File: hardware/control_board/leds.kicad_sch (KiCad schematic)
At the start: 17 parts, among them Q1 2N7002A

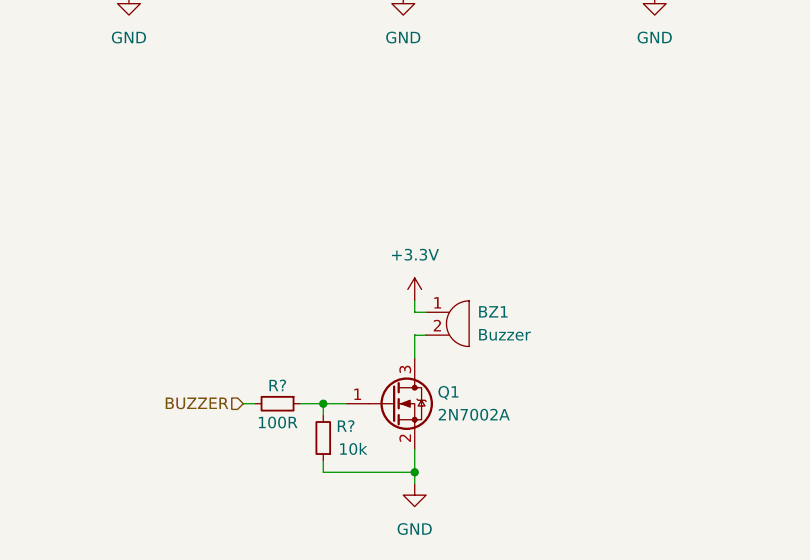
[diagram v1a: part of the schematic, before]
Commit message: Change the buzzer
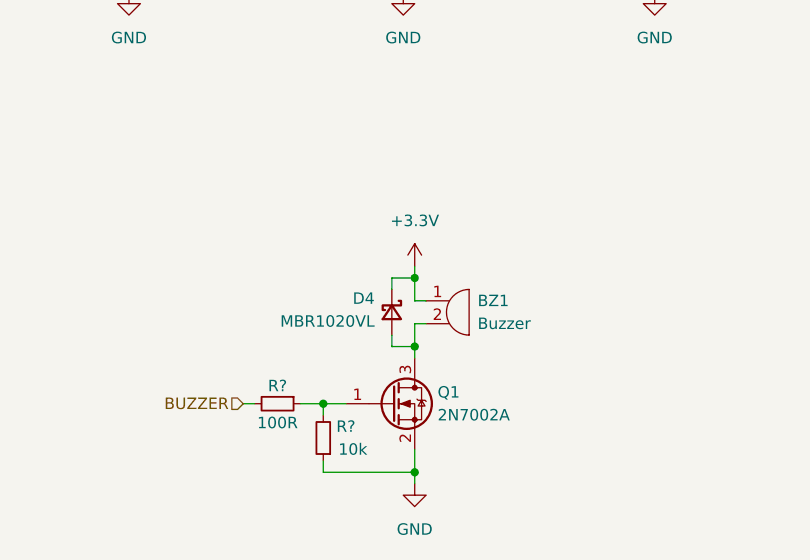
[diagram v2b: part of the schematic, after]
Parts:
- removed BZ1: Buzzer, Local_Library:PKM13EPYH4000-A0, symbol PKM13EPYH4000-A0:PKM13EPYH4000-A0
- added BZ1: Buzzer, Local_Library:CMI-9605IC-0380T, symbol CMI-9605IC-0380T:CMI-9605IC-0380T
- added D4: MBR1020VL, Diode_SMD:D_SOD-123F, symbol Device:D_Schottky_Small
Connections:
- net +3.3V: now also BZ1.1, D4.1 (K)
- net at Q1.3 (D): now also BZ1.2, D4.2 (A)
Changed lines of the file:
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@@
     (comment 1 "Promoter: A. Bondyra, Ph.D.")
   )
+  (junction (at 139.7 130.81) (diameter 0) (color 0 0 0 0)
+  )
   (junction (at 139.7 144.78) (diameter 0) (color 0 0 0 0)
   )
   (junction (at 129.54 137.16) (diameter 0) (color 0 0 0 0)
   )
+  (junction (at 139.7 123.19) (diameter 0) (color 0 0 0 0)
+  )
   (wire (pts (xy 80.01 93.98) (xy 80.01 95.25))
     (stroke (width 0) (type default))
@@
     (stroke (width 0) (type default))
   )
-  (wire (pts (xy 140.97 127) (xy 139.7 127))
-    (stroke (width 0) (type default))
-  )
-  (wire (pts (xy 139.7 129.54) (xy 140.97 129.54))
+  (wire (pts (xy 137.16 123.19) (xy 137.16 124.46))
+    (stroke (width 0) (type default))
+  )
+  (wire (pts (xy 137.16 130.81) (xy 139.7 130.81))
+    (stroke (width 0) (type default))
+  )
+  (wire (pts (xy 140.97 125.73) (xy 139.7 125.73))
+    (stroke (width 0) (type default))
+  )
+  (wire (pts (xy 139.7 128.27) (xy 140.97 128.27))
+    (stroke (width 0) (type default))
+  )
+  (wire (pts (xy 139.7 123.19) (xy 139.7 125.73))
+    (stroke (width 0) (type default))
+  )
+  (wire (pts (xy 139.7 128.27) (xy 139.7 130.81))
     (stroke (width 0) (type default))
   )
@@
     (stroke (width 0) (type default))
   )
+  (wire (pts (xy 137.16 123.19) (xy 139.7 123.19))
+    (stroke (width 0) (type default))
+  )
   (wire (pts (xy 127 137.16) (xy 129.54 137.16))
     (stroke (width 0) (type default))
@@
     (stroke (width 0) (type default))
   )
-  (wire (pts (xy 139.7 127) (xy 139.7 125.73))
-    (stroke (width 0) (type default))
-  )
   (wire (pts (xy 219.71 90.17) (xy 219.71 91.44))
     (stroke (width 0) (type default))
@@
     (stroke (width 0) (type default))
   )
+  (wire (pts (xy 139.7 121.92) (xy 139.7 123.19))
+    (stroke (width 0) (type default))
+  )
   (wire (pts (xy 193.04 74.93) (xy 194.31 74.93))
     (stroke (width 0) (type default))
@@
     (stroke (width 0) (type default))
   )
+  (wire (pts (xy 139.7 130.81) (xy 139.7 132.08))
+    (stroke (width 0) (type default))
+  )
   (wire (pts (xy 139.7 144.78) (xy 139.7 146.05))
     (stroke (width 0) (type default))
@@
     (stroke (width 0) (type default))
   )
+  (wire (pts (xy 137.16 130.81) (xy 137.16 129.54))
+    (stroke (width 0) (type default))
+  )
   (wire (pts (xy 138.43 90.17) (xy 138.43 91.44))
     (stroke (width 0) (type default))
@@
   )
   (wire (pts (xy 80.01 74.93) (xy 80.01 76.2))
-    (stroke (width 0) (type default))
-  )
-  (wire (pts (xy 139.7 129.54) (xy 139.7 132.08))
     (stroke (width 0) (type default))
   )
@@
     )
   )
-  (symbol (lib_id "PKM13EPYH4000-A0:PKM13EPYH4000-A0") (at 143.51 128.27 0) (unit 1)
-    (in_bom yes) (on_board yes) (dnp no)
-    (property "Reference" "BZ1" (at 146.685 127 0)
-      (effects (font (size 1.27 1.27)) (justify left))
-    )
-    (property "Value" "Buzzer" (at 146.685 129.54 0)
-      (effects (font (size 1.27 1.27)) (justify left))
-    )
-    (property "Footprint" "Local_Library:PKM13EPYH4000-A0" (at 142.875 135.89 0)
-      (effects (font (size 1.27 1.27)) hide)
-    )
-    (property "Datasheet" "https://www.murata.com/en-us/api/pdfdownloadapi?cate=&partno=PKM13EPYH4000-A0" (at 142.875 138.43 0)
-      (effects (font (size 1.27 1.27)) hide)
-    )
-    (property "Component" "PKM13EPYH4000-A0" (at 143.51 128.27 0)
-      (effects (font (size 1.27 1.27)) hide)
-    )
-    (pin "1")
-    (pin "2")
-    (instances
-      (project "control_board"
-        (path "/b652b05a-4e3d-4ad1-b032-18886abe7d45"
-          (reference "BZ1") (unit 1)
-        )
-        (path "/b652b05a-4e3d-4ad1-b032-18886abe7d45/1df5b500-a950-4c3c-8279-0c408859e423"
-          (reference "BZ1") (unit 1)
-        )
-      )
-    )
-  )
   (symbol (lib_id "Device:R_Small") (at 107.95 81.28 0) (mirror y) (unit 1)
     (in_bom yes) (on_board yes) (dnp no)
@@
         )
         (path "/b652b05a-4e3d-4ad1-b032-18886abe7d45/1df5b500-a950-4c3c-8279-0c408859e423"
-          (reference "R17") (unit 1)
+          (reference "R16") (unit 1)
         )
       )
@@
         )
         (path "/b652b05a-4e3d-4ad1-b032-18886abe7d45/1df5b500-a950-4c3c-8279-0c408859e423"
-          (reference "R19") (unit 1)
+          (reference "R18") (unit 1)
         )
       )
@@
         )
         (path "/b652b05a-4e3d-4ad1-b032-18886abe7d45/1df5b500-a950-4c3c-8279-0c408859e423"
-          (reference "R23") (unit 1)
+          (reference "R22") (unit 1)
         )
       )
@@
         )
         (path "/b652b05a-4e3d-4ad1-b032-18886abe7d45/1df5b500-a950-4c3c-8279-0c408859e423"
-          (reference "R16") (unit 1)
+          (reference "R15") (unit 1)
         )
       )
@@
         )
         (path "/b652b05a-4e3d-4ad1-b032-18886abe7d45/1df5b500-a950-4c3c-8279-0c408859e423"
-          (reference "D6") (unit 1)
+          (reference "D7") (unit 1)
         )
       )
@@
     )
   )
-  (symbol (lib_id "power:+3.3V") (at 139.7 125.73 0) (unit 1)
-    (in_bom yes) (on_board yes) (dnp no)
-    (property "Reference" "#PWR?" (at 139.7 129.54 0)
-      (effects (font (size 1.27 1.27)) hide)
-    )
-    (property "Value" "+3.3V" (at 139.7 120.65 0)
+  (symbol (lib_id "power:+3.3V") (at 139.7 121.92 0) (unit 1)
+    (in_bom yes) (on_board yes) (dnp no)
+    (property "Reference" "#PWR?" (at 139.7 125.73 0)
+      (effects (font (size 1.27 1.27)) hide)
+    )
+    (property "Value" "+3.3V" (at 139.7 116.84 0)
       (effects (font (size 1.27 1.27)))
     )
-    (property "Footprint" "" (at 139.7 125.73 0)
-      (effects (font (size 1.27 1.27)) hide)
-    )
-    (property "Datasheet" "" (at 139.7 125.73 0)
+    (property "Footprint" "" (at 139.7 121.92 0)
+      (effects (font (size 1.27 1.27)) hide)
+    )
+    (property "Datasheet" "" (at 139.7 121.92 0)
       (effects (font (size 1.27 1.27)) hide)
     )
@@
         )
         (path "/b652b05a-4e3d-4ad1-b032-18886abe7d45/1df5b500-a950-4c3c-8279-0c408859e423"
-          (reference "R18") (unit 1)
+          (reference "R17") (unit 1)
         )
       )
@@
     )
   )
+  (symbol (lib_id "Device:D_Schottky_Small") (at 137.16 127 270) (unit 1)
+    (in_bom yes) (on_board yes) (dnp no)
+    (property "Reference" "D4" (at 135.255 125.476 90)
+      (effects (font (size 1.27 1.27)) (justify right))
+    )
+    (property "Value" "MBR1020VL" (at 135.255 128.016 90)
+      (effects (font (size 1.27 1.27)) (justify right))
+    )
+    (property "Footprint" "Diode_SMD:D_SOD-123F" (at 137.16 127 90)
+      (effects (font (size 1.27 1.27)) hide)
+    )
+    (property "Datasheet" "https://www.mouser.pl/datasheet/2/1057/MBR1020VL-1869911.pdf" (at 137.16 127 90)
+      (effects (font (size 1.27 1.27)) hide)
+    )
+    (pin "1")
+    (pin "2")
+    (instances
+      (project "control_board"
+        (path "/b652b05a-4e3d-4ad1-b032-18886abe7d45/1df5b500-a950-4c3c-8279-0c408859e423"
+          (reference "D4") (unit 1)
+        )
+      )
+    )
+  )
   (symbol (lib_id "Device:R_Small") (at 194.31 81.28 0) (mirror y) (unit 1)
     (in_bom yes) (on_board yes) (dnp no)
@@
         )
         (path "/b652b05a-4e3d-4ad1-b032-18886abe7d45/1df5b500-a950-4c3c-8279-0c408859e423"
-          (reference "R22") (unit 1)
+          (reference "R21") (unit 1)
         )
       )
@@
         )
         (path "/b652b05a-4e3d-4ad1-b032-18886abe7d45/1df5b500-a950-4c3c-8279-0c408859e423"
-          (reference "D4") (unit 1)
+          (reference "D5") (unit 1)
         )
       )
@@
         )
         (path "/b652b05a-4e3d-4ad1-b032-18886abe7d45/1df5b500-a950-4c3c-8279-0c408859e423"
-          (reference "R21") (unit 1)
+          (reference "R20") (unit 1)
         )
       )
@@
         )
         (path "/b652b05a-4e3d-4ad1-b032-18886abe7d45/1df5b500-a950-4c3c-8279-0c408859e423"
-          (reference "R20") (unit 1)
+          (reference "R19") (unit 1)
         )
       )
@@
     )
   )
+  (symbol (lib_id "CMI-9605IC-0380T:CMI-9605IC-0380T") (at 143.51 127 0) (unit 1)
+    (in_bom yes) (on_board yes) (dnp no)
+    (property "Reference" "BZ1" (at 146.685 125.73 0)
+      (effects (font (size 1.27 1.27)) (justify left))
+    )
+    (property "Value" "Buzzer" (at 146.685 128.27 0)
+      (effects (font (size 1.27 1.27)) (justify left))
+    )
+    (property "Footprint" "Local_Library:CMI-9605IC-0380T" (at 142.875 134.62 0)
+      (effects (font (size 1.27 1.27)) hide)
+    )
+    (property "Datasheet" "https://www.cuidevices.com/product/resource/cmi-9605ic-0380t.pdf" (at 142.875 137.16 0)
+      (effects (font (size 1.27 1.27)) hide)
+    )
+    (pin "2")
+    (pin "1")
+    (instances
+      (project "control_board"
+        (path "/b652b05a-4e3d-4ad1-b032-18886abe7d45/1df5b500-a950-4c3c-8279-0c408859e423"
+          (reference "BZ1") (unit 1)
+        )
+      )
+    )
+  )
   (symbol (lib_id "Device:LED_Small") (at 219.71 87.63 270) (mirror x) (unit 1)
     (in_bom yes) (on_board yes) (dnp no)
@@
         )
         (path "/b652b05a-4e3d-4ad1-b032-18886abe7d45/1df5b500-a950-4c3c-8279-0c408859e423"
-          (reference "D7") (unit 1)
+          (reference "D8") (unit 1)
         )
       )
@@
         )
         (path "/b652b05a-4e3d-4ad1-b032-18886abe7d45/1df5b500-a950-4c3c-8279-0c408859e423"
-          (reference "D5") (unit 1)
-        )
-      )
+          (reference "D6") (unit 1)
+        )
+      )

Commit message: Fix the sheet name
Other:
- title: LED & Buzzer -> LEDs & Buzzer
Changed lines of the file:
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@@
   (paper "A4")
   (title_block
-    (title "LED & Buzzer")
+    (title "LEDs & Buzzer")
     (date "2023-11-29")
     (rev "${REVISION}")

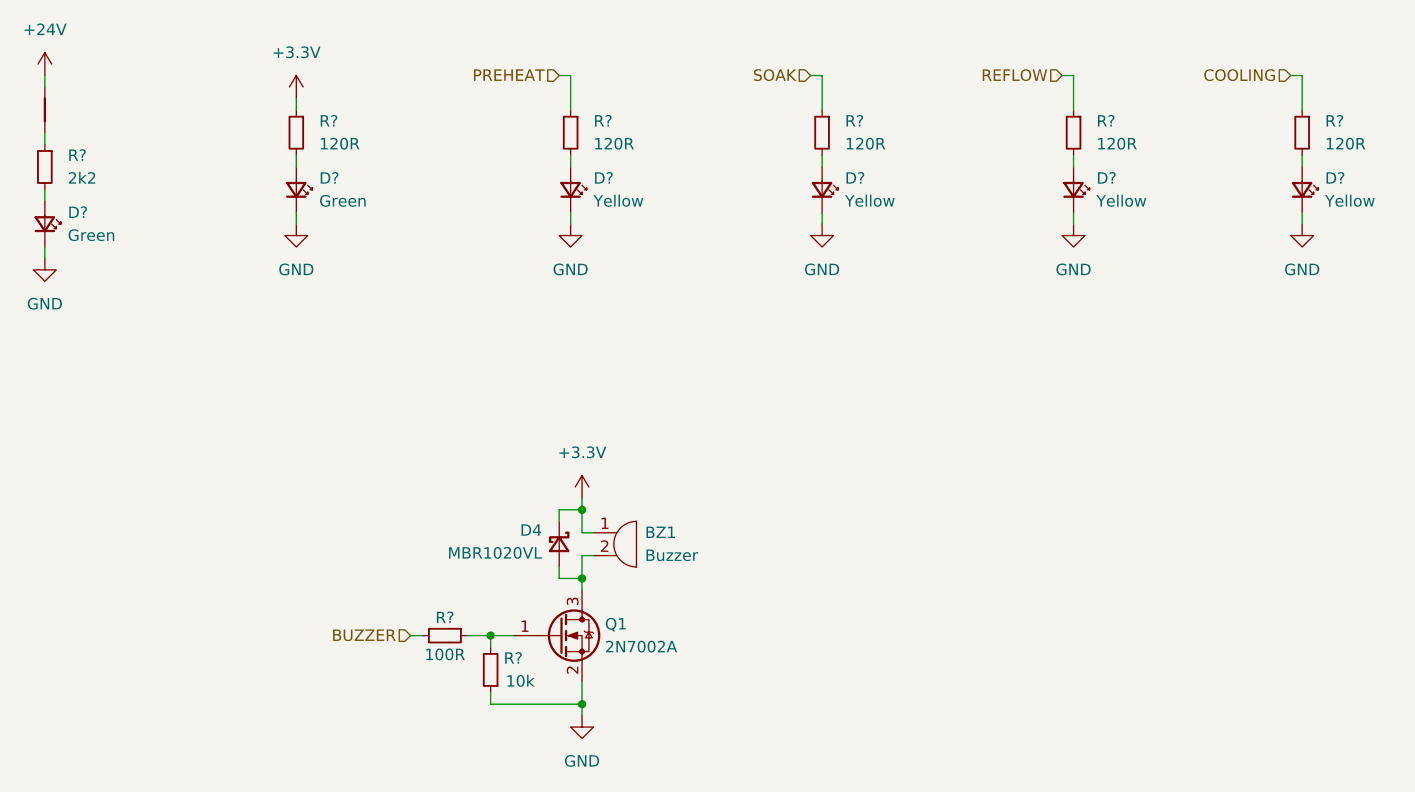
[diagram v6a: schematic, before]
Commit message: Update reference designators
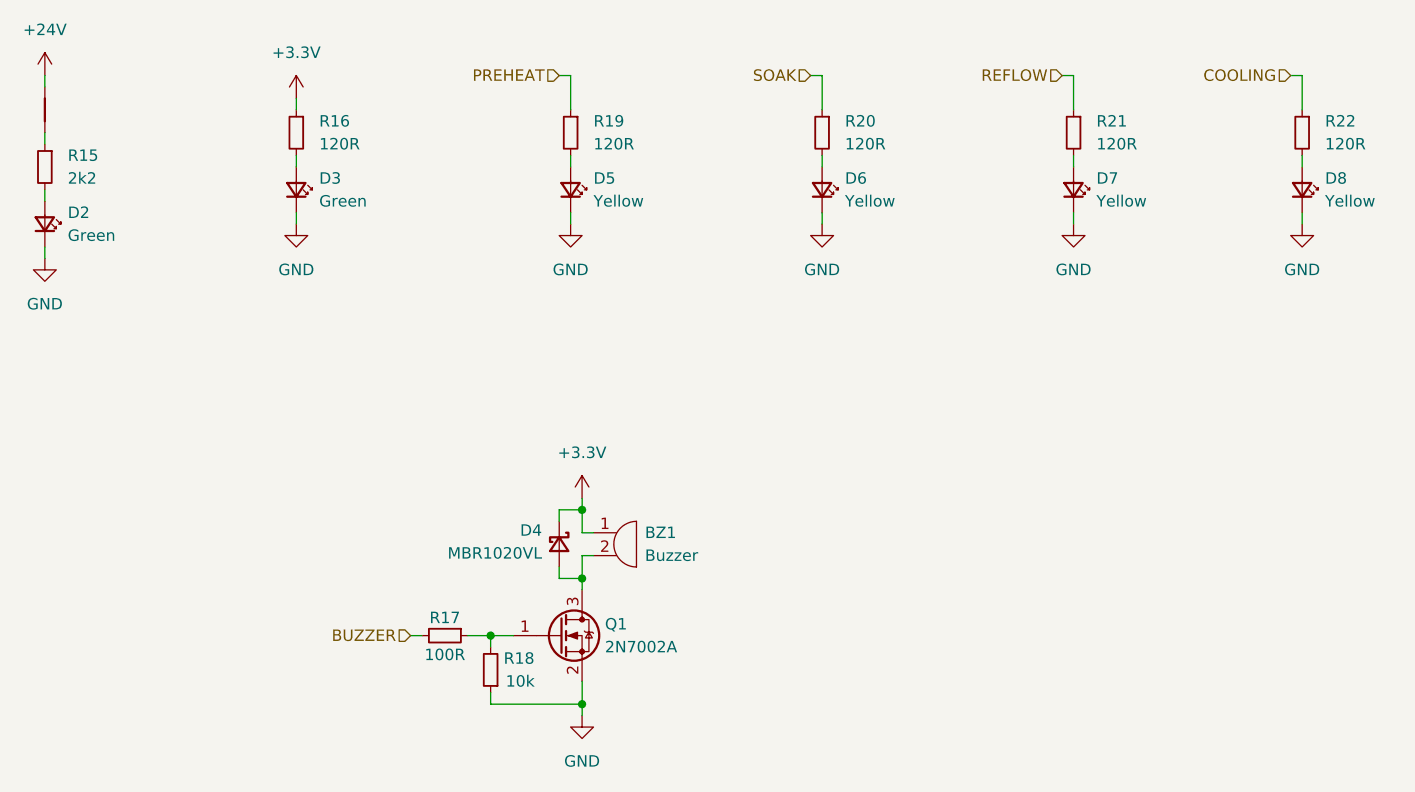
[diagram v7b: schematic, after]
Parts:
- gave numbers to parts that had none: 14
